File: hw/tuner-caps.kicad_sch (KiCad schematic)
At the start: 28 parts, among them K2101 G2RL-2, K2102 G2RL-2, K2103 G2RL-2, K2104 G2RL-2, K2105 G2RL-2, K2106 G2RL-2, K2107 G2RL-2, K2108 G2RL-2, K2109 G2RL-2, U2101 TLC6C598PW, U2102 TLC6C598PW

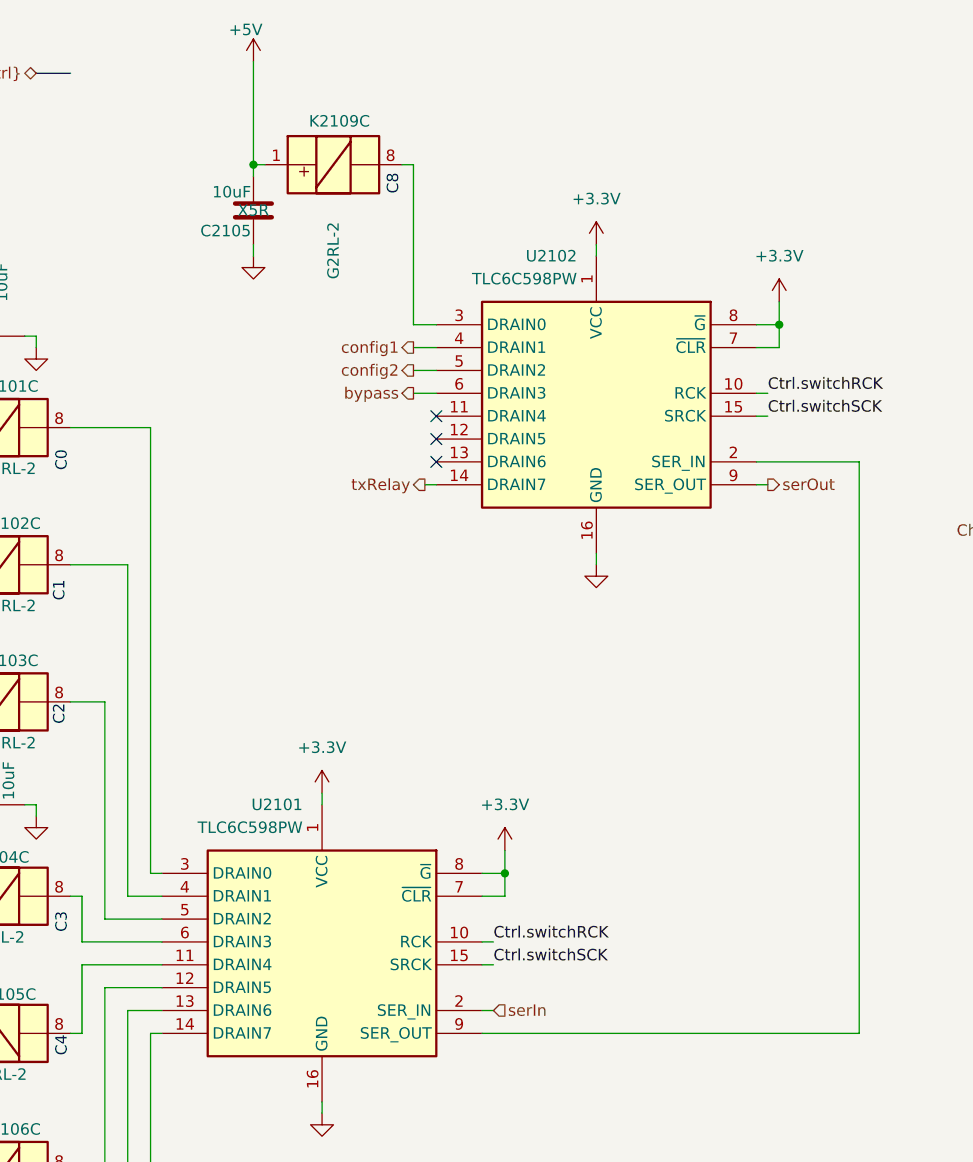
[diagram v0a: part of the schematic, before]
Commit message: Have to use 5V signaling for relay drivers (ick). Add level shifter for that too. STM32 pins were way out of control. I think I got it all back together. Probably still need relay flyback snubber diodes in some places.
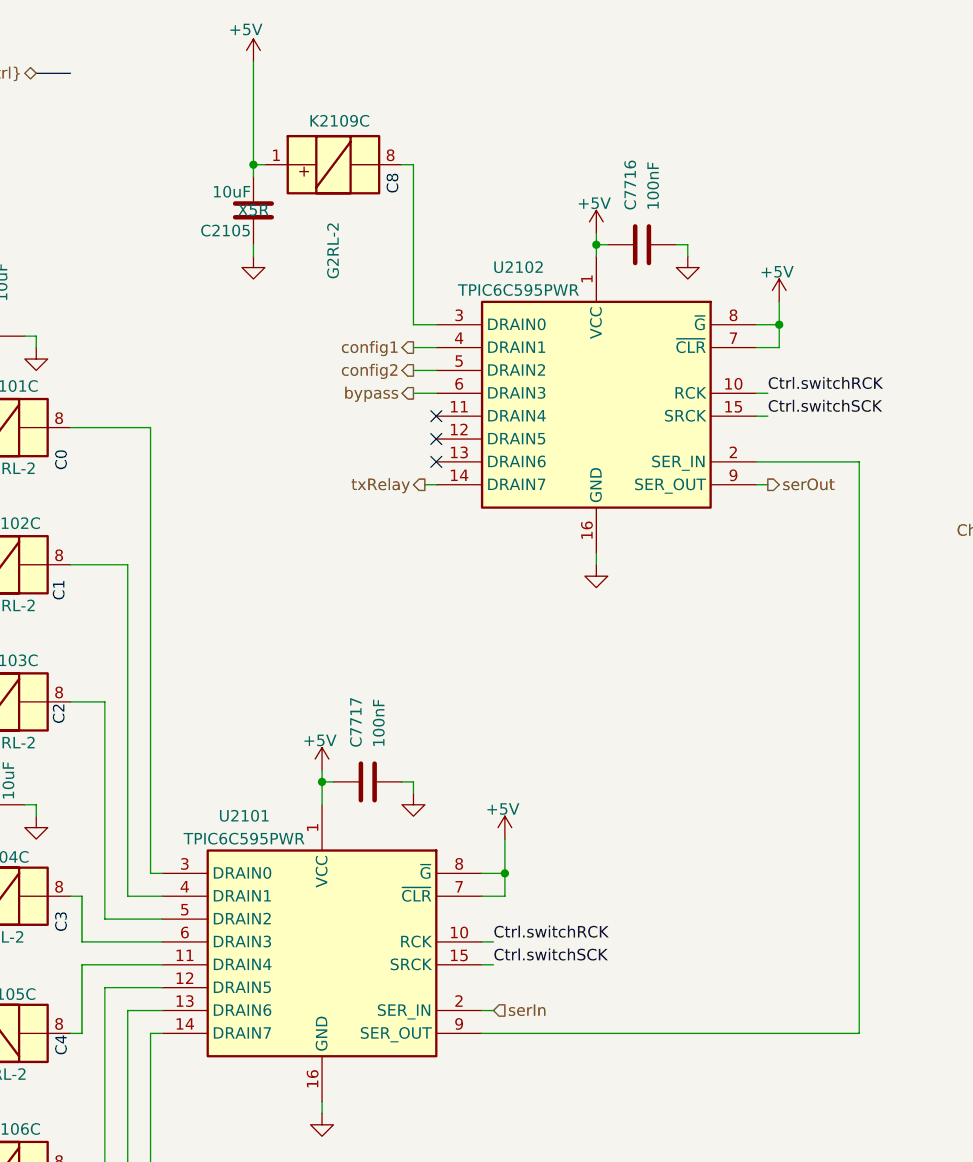
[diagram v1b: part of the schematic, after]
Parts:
- removed U2101, U2102: TLC6C598PW, Package_SO:TSSOP-16_4.4x5mm_P0.65mm, symbol Library:TLC6C598PW
- added C7716, C7717: 100nF, Capacitor_SMD:C_0603_1608Metric, symbol Device:C
- added U2101, U2102: TPIC6C595PWR, SOP65P640X120-16N, symbol Library:TPIC6C595PWR
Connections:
- net +5V: now also C7716.1, C7717.1, U2101.1 (VCC), U2101.7 (~{CLR}), U2101.8 (~{G}), U2102.1 (VCC), U2102.7 (~{CLR}), U2102.8 (~{G})
- net Ctrl.switchRCK: now also U2101.10 (RCK), U2102.10 (RCK)
- net Ctrl.switchSCK: now also U2101.15 (SRCK), U2102.15 (SRCK)
- net GND: now also C7716.2, C7717.2, U2101.16 (GND), U2102.16 (GND)
- net bypass: now also U2102.6 (DRAIN3)
- net config1: now also U2102.4 (DRAIN1)
- net config2: now also U2102.5 (DRAIN2)
- net serIn: now also U2101.2 (SER_IN)
- net serOut: now also U2102.9 (SER_OUT)
- net txRelay: now also U2102.14 (DRAIN7)
- net at K2102.8: now also U2101.4 (DRAIN1)
- net at K2108.8: now also U2101.14 (DRAIN7)
- net at K2101.8: now also U2101.3 (DRAIN0)
- net at K2107.8: now also U2101.13 (DRAIN6)
- net at K2109.8: now also U2102.3 (DRAIN0)
- net at K2105.8: now also U2101.11 (DRAIN4)
- net at K2106.8: now also U2101.12 (DRAIN5)
- net at K2103.8: now also U2101.5 (DRAIN2)
- net at K2104.8: now also U2101.6 (DRAIN3)
- new net: U2101.9 (SER_OUT), U2102.2 (SER_IN)

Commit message: I think I have finished the relay conversion and 5V SPI I/O expander crap
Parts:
- removed C2101, C2102, C2103, C2104, C2105, C2107: 10uF, Capacitor_SMD:C_0805_2012Metric, symbol Device:C
- removed C2106, C2108: 100nF, Capacitor_SMD:C_0805_2012Metric, symbol Device:C
- removed C7716: 100nF, Capacitor_SMD:C_0603_1608Metric, symbol Device:C
- removed K2101, K2102, K2103, K2104, K2105, K2106, K2107, K2108, K2109: G2RL-2, Library:Relay_DPDT_Omron_G2RL-2, symbol Library:G2RL-2-functional
- removed U2102: TPIC6C595PWR, SOP65P640X120-16N, symbol Library:TPIC6C595PWR
- added D7717, D7718, D7719, D7720, D7721, D7722, D7723, D7724, D7726, D7727, D7728, D7729, D7730, D7731, D7732, D7733, D7734, D7735: 1N4148W, Diode_SMD:D_SOD-123, symbol Diode:1N4148W
- added K7725, K7726, K7727, K7728, K7729, K7730, K7731, K7732, K7733, K7734, K7735, K7736, K7737, K7738, K7739, K7740, K7741, K7742: G5Q-14-05, Relay_THT:Relay_SPDT_Omron-G5Q-1, symbol Relay:G5Q-1
- C7938: renamed from C2121; working-voltage 500V -> 1kV
- renumbered C2117 to C7939, C2120 to C7940, C2116 to C7941, C2119 to C7942, C2114 to C7943, C2118 to C7945, C2113 to C7946, C2110 to C7949, C7717 to C7951, U2101 to U7755
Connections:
- net +5V: now also D7717.1 (K), D7718.1 (K), D7719.1 (K), D7720.1 (K), D7721.1 (K), D7722.1 (K), D7723.1 (K), D7724.1 (K), D7726.1 (K), D7727.1 (K), D7728.1 (K), D7729.1 (K), D7730.1 (K), D7731.1 (K), D7732.1 (K), D7733.1 (K), D7734.1 (K), D7735.1 (K), K7725.5, K7726.5, K7727.5, K7728.5, K7729.5, K7730.5, K7731.5, K7732.5, K7733.5, K7734.5, K7735.5, K7736.5, K7737.5, K7738.5, K7739.5, K7740.5, K7741.5, K7742.5
- net Ccold: now also K7726.3, K7728.3, K7730.3, K7732.3, K7734.3, K7736.3, K7738.3, K7740.3, K7742.3
- net Chot: now also K7725.3, K7727.3, K7729.3, K7731.3, K7733.3, K7735.3, K7737.3, K7739.3, K7741.3
- net GND: now also K7725.4, K7726.4, K7727.4, K7728.4, K7729.4, K7730.4, K7731.4, K7732.4, K7733.4, K7734.4, K7735.4, K7736.4, K7737.4, K7738.4, K7739.4, K7740.4, K7741.4, K7742.4
- net serOut: now also U7755.9 (SER_OUT)
- net at C7949.1: now also K7741.2
- net at C7949.2: now also K7742.2
- net at C7942.1: now also K7733.2
- net at C7942.2: now also K7734.2
- net at C7941.1: now also K7731.2
- net at C7941.2: now also K7732.2
- net at C7943.1: now also K7735.2
- net at C7943.2: now also K7736.2
- net C1: now reaches U7755.4 (DRAIN1)
- net C1: now also D7722.2 (A), D7724.2 (A), K7730.1, K7732.1
- net at C7938.1: now also K7725.2
- net at C7938.2: now also K7726.2
- net at C7939.1: now also K7727.2
- net at C7939.2: now also K7728.2
- net C7: now reaches U7755.14 (DRAIN7)
- net C0: now reaches U7755.3 (DRAIN0)
- net C0: now also D7718.2 (A), D7720.2 (A), K7726.1, K7728.1
- net at C7946.1: now also K7739.2
- net at C7946.2: now also K7740.2
- net at C7940.2: now also K7730.2
- net at C7940.1: now also K7729.2
- net C6: now reaches U7755.13 (DRAIN6)
- net at C7945.1: now also K7737.2
- net at C7945.2: now also K7738.2
- net C5: now reaches U7755.12 (DRAIN5)
- net C4: now reaches U7755.11 (DRAIN4)
- net C2: now reaches U7755.5 (DRAIN2)
- net C2: now also D7727.2 (A), D7729.2 (A), K7734.1, K7736.1
- net C3: now reaches U7755.6 (DRAIN3)
- net C3: now also D7731.2 (A), D7733.2 (A), K7738.1, K7740.1
- new net: D7717.2 (A), K7725.1
- new net: D7719.2 (A), K7727.1
- new net: D7732.2 (A), K7739.1
- new net: D7730.2 (A), K7737.1
- new net: D7723.2 (A), K7731.1
- new net: D7721.2 (A), K7729.1
- new net: D7728.2 (A), K7735.1
- new net: D7726.2 (A), K7733.1
- new net: D7734.2 (A), K7741.1
- new net C8: D7735.2 (A), K7742.1
- no-connect marks 12 -> 0
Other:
- note removed: "C0"
- note removed: "C1"
- note removed: "C2"
- note removed: "C3"
- note removed: "C4"
- note removed: "C5"
- note removed: "C6"
- note removed: "C7"
- note removed: "C8"
- moved on the sheet: C7938, C7939, C7940, C7941, C7942, C7943, C7945, C7946, C7949, C7951, U7755

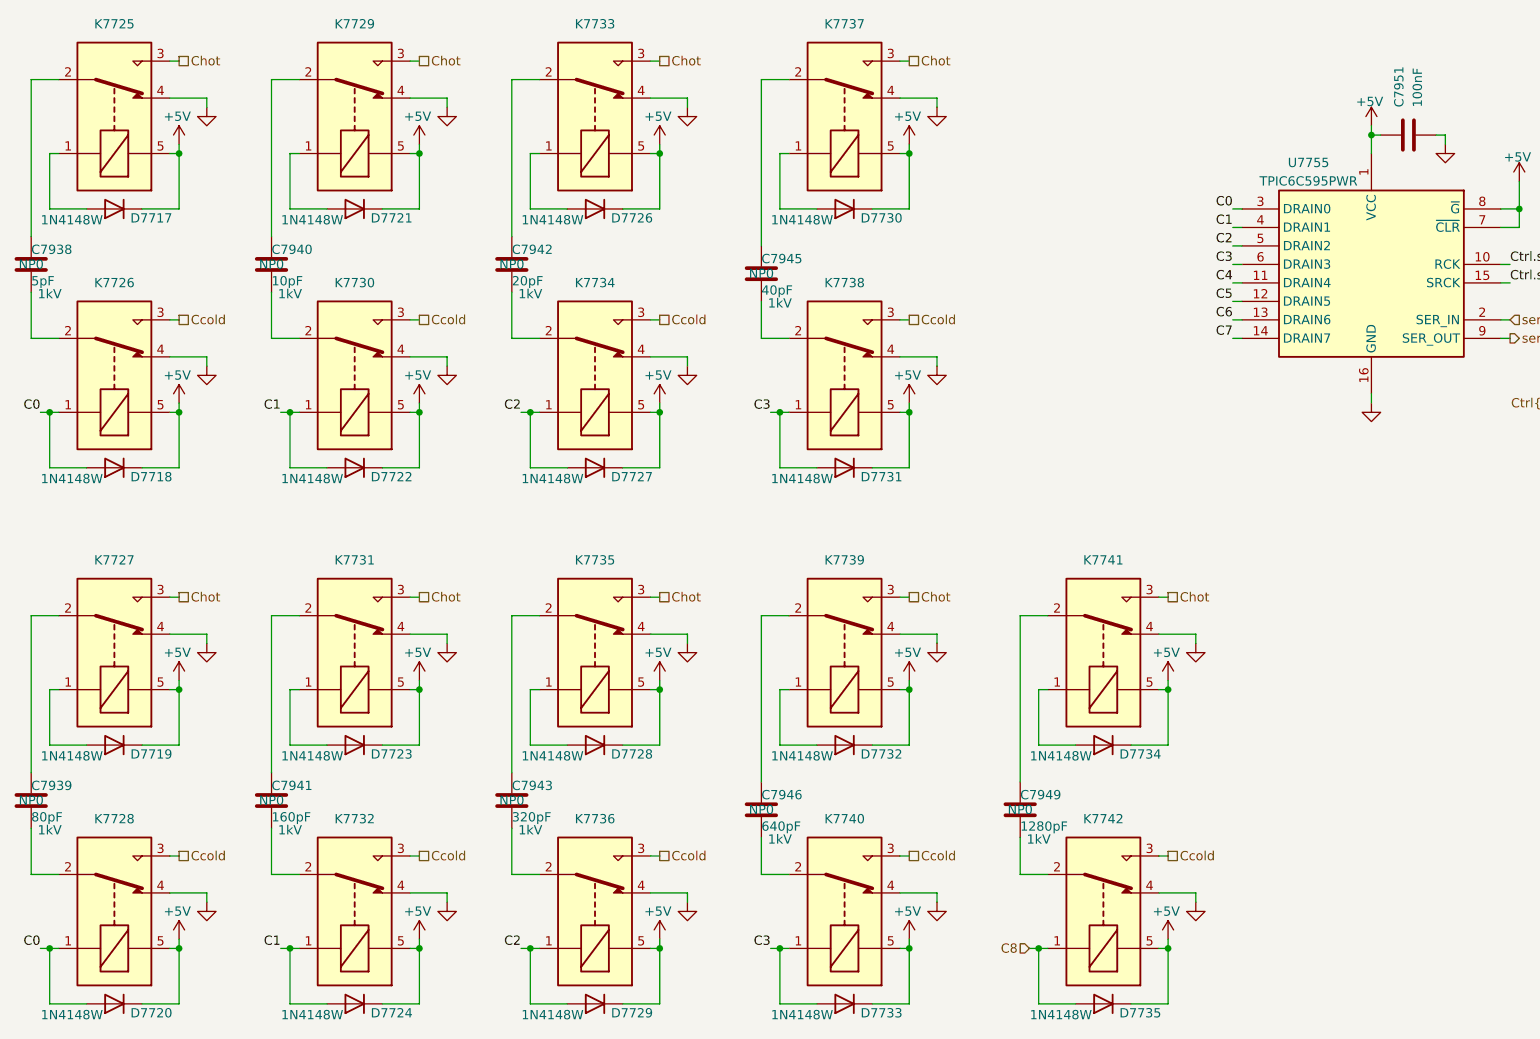
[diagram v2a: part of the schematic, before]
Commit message: Starting to build guanella transformers. Mostly converted to 1-2-1 tx, but FPGA still to do.
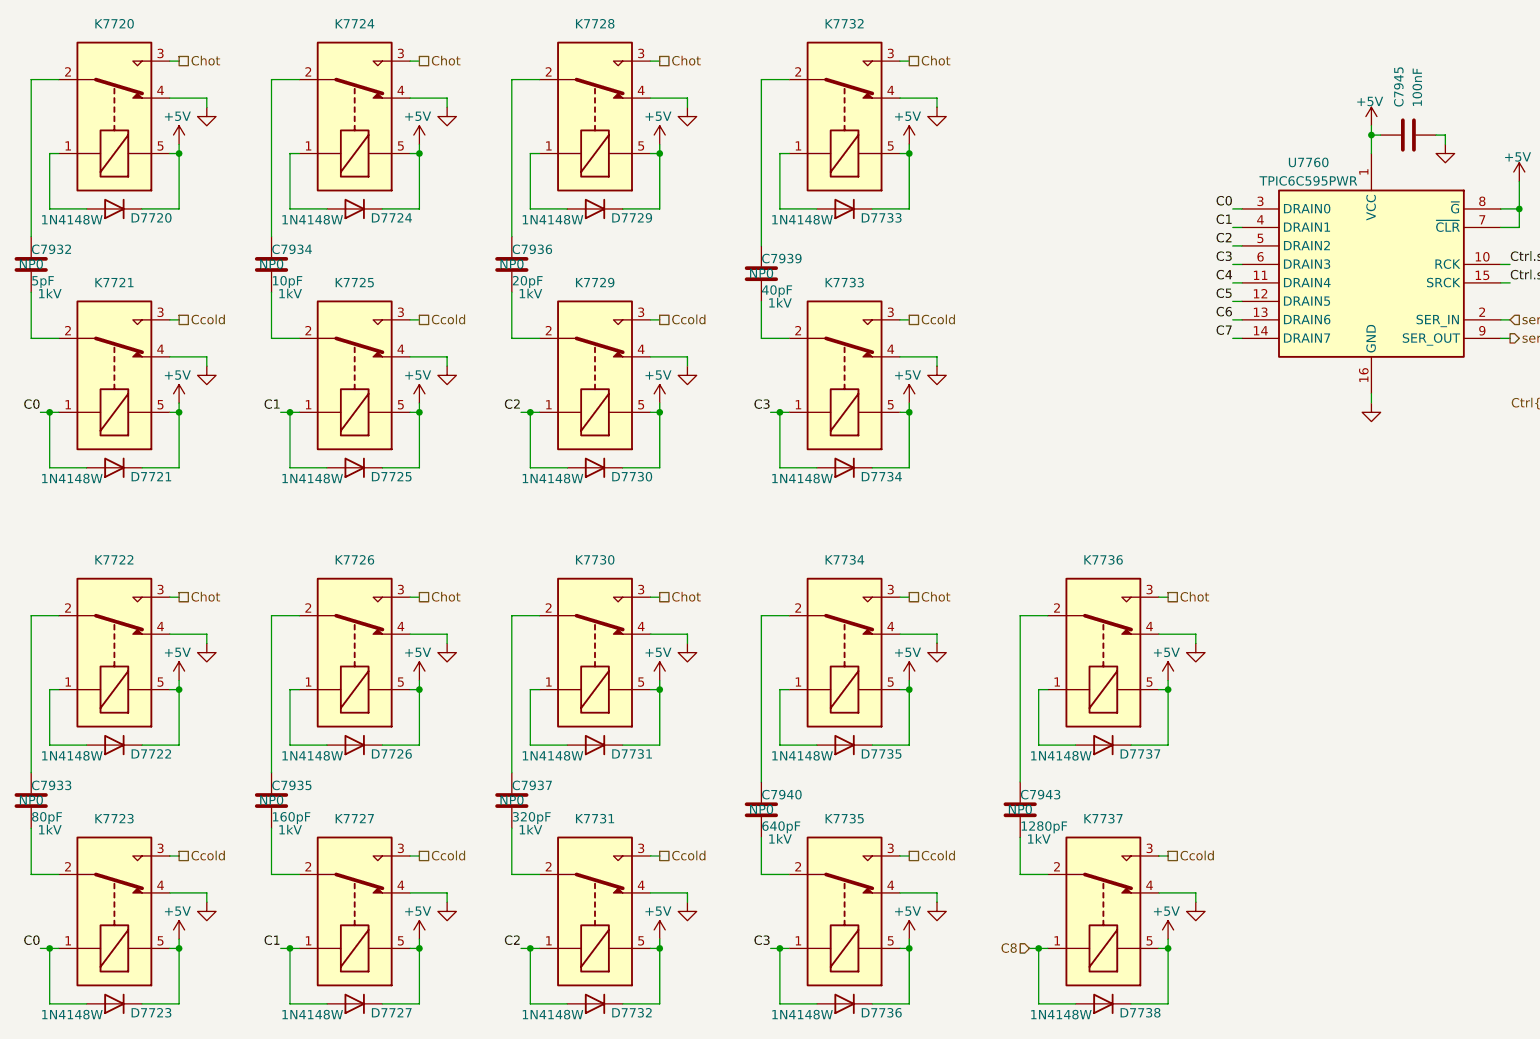
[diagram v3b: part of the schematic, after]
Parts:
- renumbered C7938 to C7932, C7939 to C7933, C7940 to C7934, C7941 to C7935, C7942 to C7936, C7943 to C7937, C7945 to C7939, C7946 to C7940, C7949 to C7943, C7951 to C7945, D7717 to D7720, D7718 to D7721, D7719 to D7722, D7720 to D7723, D7721 to D7724, D7722 to D7725, D7723 to D7726, D7724 to D7727, D7726 to D7729, D7727 to D7730, D7728 to D7731, D7729 to D7732, D7730 to D7733, D7731 to D7734, D7732 to D7735, D7733 to D7736, D7734 to D7737, D7735 to D7738, K7725 to K7720, K7726 to K7721, K7727 to K7722, K7728 to K7723, K7729 to K7724, K7730 to K7725, K7731 to K7726, K7732 to K7727, K7733 to K7728, K7734 to K7729, K7735 to K7730, K7736 to K7731, K7737 to K7732, K7738 to K7733, K7739 to K7734, K7740 to K7735, K7741 to K7736, K7742 to K7737, U7755 to U7760

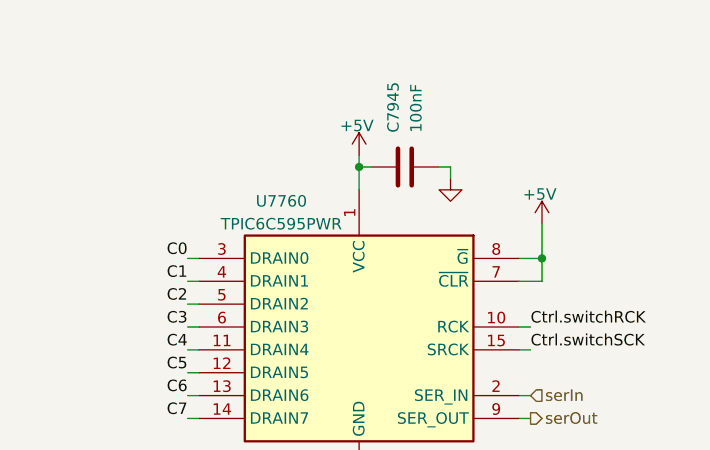
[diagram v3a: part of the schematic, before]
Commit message: Checkpoint. FPGA is mostly done (need a check!). Working on new LPFs. Need inductor footprints and to fix a bunch of broken/missing footprints.
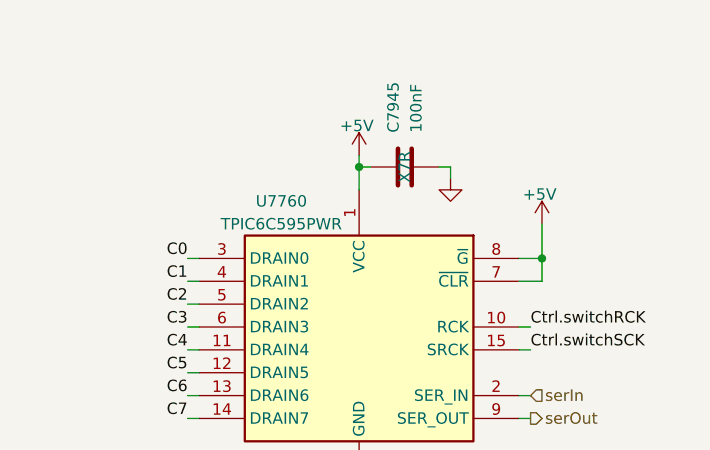
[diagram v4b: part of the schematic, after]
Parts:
- C7932, C7933, C7934, C7935, C7936, C7937, C7939, C7940, C7943: footprint Capacitor_SMD:C_0201_0603Metric -> Capacitor_SMD:C_0603_1608Metric
- C7945: cap-type (none) -> X7R
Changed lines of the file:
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@@
 			)
 		)
-		(property "Footprint" "Capacitor_SMD:C_0201_0603Metric"
+		(property "Footprint" "Capacitor_SMD:C_0603_1608Metric"
 			(at 155.9052 128.27 0)
 			(effects
@@
 			)
 		)
-		(property "Footprint" "Capacitor_SMD:C_0201_0603Metric"
+		(property "Footprint" "Capacitor_SMD:C_0603_1608Metric"
 			(at 86.0552 53.34 0)
 			(effects
@@
 			)
 		)
-		(property "Footprint" "Capacitor_SMD:C_0201_0603Metric"
+		(property "Footprint" "Capacitor_SMD:C_0603_1608Metric"
 			(at 53.0352 127 0)
 			(effects
@@
 			)
 		)
-		(property "Footprint" "Capacitor_SMD:C_0201_0603Metric"
+		(property "Footprint" "Capacitor_SMD:C_0603_1608Metric"
 			(at 86.0552 127 0)
 			(effects
@@
 			)
 		)
-		(property "Footprint" "Capacitor_SMD:C_0201_0603Metric"
+		(property "Footprint" "Capacitor_SMD:C_0603_1608Metric"
 			(at 20.0152 53.34 0)
 			(effects
@@
 			)
 		)
-		(property "Footprint" "Capacitor_SMD:C_0201_0603Metric"
+		(property "Footprint" "Capacitor_SMD:C_0603_1608Metric"
 			(at 20.0152 127 0)
 			(effects
@@
 			)
 		)
-		(property "Footprint" "Capacitor_SMD:C_0201_0603Metric"
+		(property "Footprint" "Capacitor_SMD:C_0603_1608Metric"
 			(at 120.3452 128.27 0)
 			(effects
@@
 			)
 		)
-		(property "cap-type" ""
+		(property "cap-type" "X7R"
 			(at 208.28 31.75 0)
 			(effects
@@
 			)
 		)
-		(property "Footprint" "Capacitor_SMD:C_0201_0603Metric"
+		(property "Footprint" "Capacitor_SMD:C_0603_1608Metric"
 			(at 53.0352 53.34 0)
 			(effects
@@
 			)
 		)
-		(property "Footprint" "Capacitor_SMD:C_0201_0603Metric"
+		(property "Footprint" "Capacitor_SMD:C_0603_1608Metric"
 			(at 120.3452 54.61 0)
 			(effects
